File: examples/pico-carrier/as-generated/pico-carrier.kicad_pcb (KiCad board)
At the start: 2 copper layers, 82 x 68 mm, 9 parts, among them J1 5V IN, J3 GP0-GP15, J4 GP16-GP28, PWR, U1 Pico

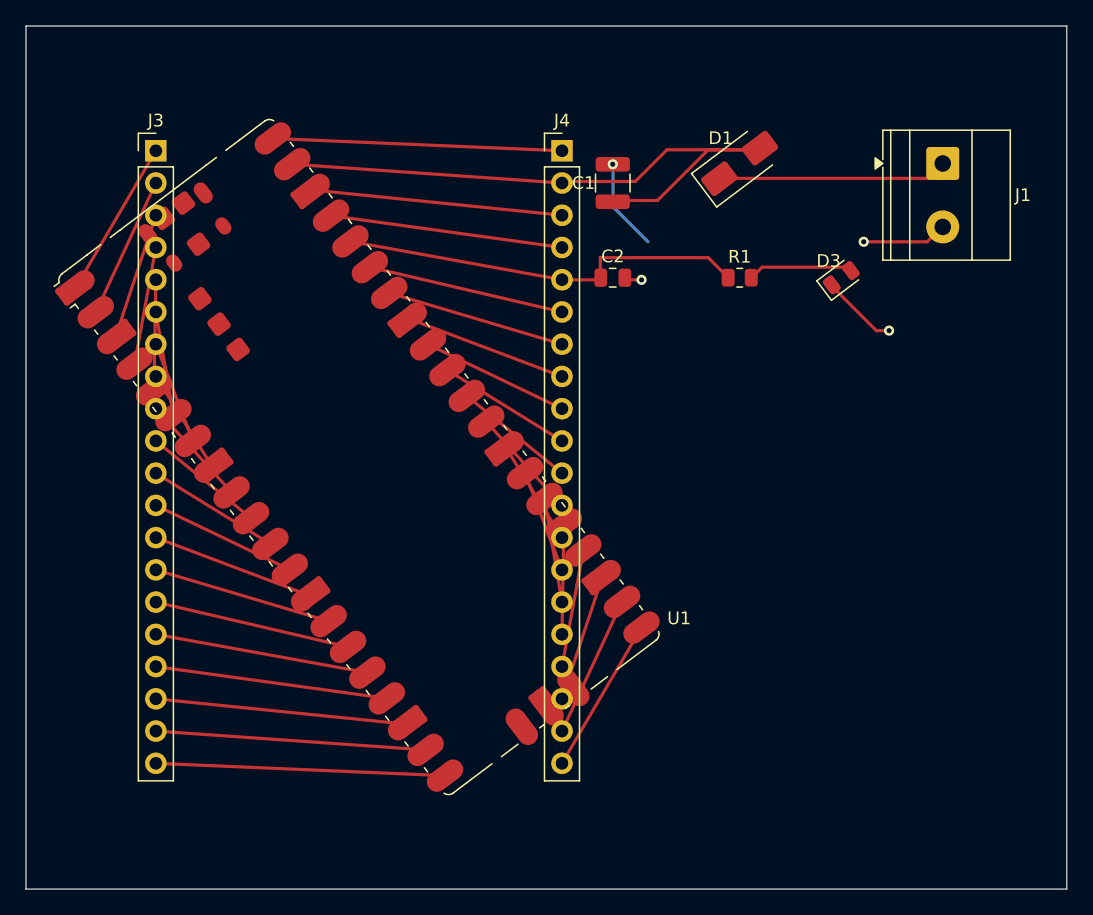
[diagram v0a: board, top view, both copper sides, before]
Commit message: Finish the fifth example, and stamp the model that wrote them
All five reviewed boards now pass KiCad's own checks: no DRC errors, nothing
unconnected, no schematic-parity findings, on 9.0.9 and 10.0.4. What is left
across the whole set is four silkscreen warnings and one library-footprint
hash, all of which come from the KiCad footprints themselves.

Getting the iCE40 board there found five things, each of which was silently
producing a board that was not the board the schematic described:

* **Two nets touching on the sheet is not something an endpoint check can
  see.** A wire that ends *on* another wire joins them, and on a sheet where
  every pin drags a stub behind it that is the common case. `schematic_shorts`
  looks for it now, and found three on this design - one of which had merged
  the 1.2 V and 3.3 V rails. The only visible sign had been KiCad's parity
  check disagreeing about a net name.
* **A symbol drawn in four units has to be placed four times.** Emitting all
  forty-eight pins under `(unit 1)` leaves three quarters of them in units
  that were never placed, which is twenty-five parity findings and a sheet
  nobody can read. The iCE40's banks and its supplies are four boxes now.
* **A pin the design does not use still has a net.** KiCad names it
  `unconnected-(U1A-IOT_37a-Pad23)`; a board that leaves the pad bare disagrees
  about every one of them.
* **A QFN counts anticlockwise**, so its east and north rows run bottom-to-top
  and right-to-left, and handing them to the fan-out in number order made
  every escape on those sides cross every other one.
* **Two rectangles that meet at a corner are further apart than growing both
  and asking whether they intersect makes them look** - which is every pair of
  pads on the corner of a QFN.

And two smaller ones: the router now keeps its vias away from every drilled
hole rather than only from its own, and the degraded variant is degraded from
the *routed* design rather than re-routed, which is both th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
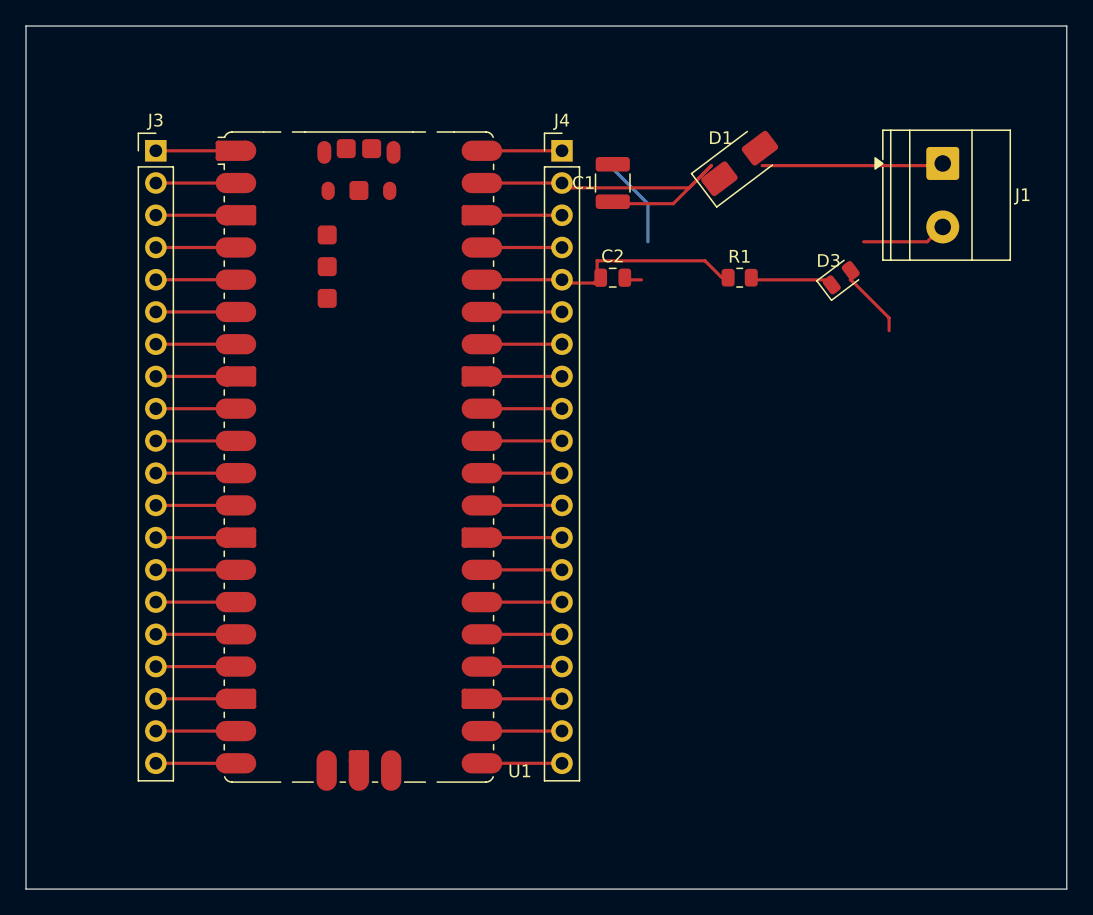
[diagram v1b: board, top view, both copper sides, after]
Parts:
- turned U1 to 0 degrees
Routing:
- net GND: track 111.0 -> 64.6 mm, vias 4 -> 0
- net /VSYS: track 51.3 -> 28.4 mm
- net /GP15: track 22.8 -> 6.31 mm
- net /VBUS: track 22.8 -> 6.31 mm
- net /GP14: track 21.3 -> 6.31 mm
- net /3V3_EN: track 18.4 -> 6.31 mm
- net /GP13: track 18.4 -> 6.31 mm
- net +3V3: track 32.3 -> 21.7 mm
- net /GP12: track 16.9 -> 6.31 mm
- net /GP11: track 15.5 -> 6.31 mm
- net /ADC_VREF: track 15.5 -> 6.31 mm
- net /GP28: track 14.2 -> 6.31 mm
- net /GP10: track 14.2 -> 6.31 mm
- net /AGND: track 12.9 -> 6.31 mm
- net /GP16: track 12.4 -> 6.31 mm
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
